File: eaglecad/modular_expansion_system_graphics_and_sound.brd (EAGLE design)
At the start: 81.4 x 100.5 mm, 63 parts, among them IC1_JOY2_BUF 74LS244N, IC2_GLU ATF22V10, IC3 74LS74N, IC8_JOY1_BUF 74LS244N, IC9-74HCU04 74LS04N, J1-INTERRUPTS INTERRUPTS, J1_ADDRESS_CON j1, J2-WAITS WAITS, J2_DATA_AND_POWER_CON j2, J3-VIDEO-OUT RCA, J4-AUDIO-LEFT RCA, J5-AUDIO-RIGHT RCA, Q2 2N2222, U11_SND1 SN76489, U1_TMS_RAM TMS4416, U2_VDP TMS9118, U3_TMS_RAM TMS4416, U4_SND2 SN76489, U5_SND3 SN76489, U6_SND4 SN76489, Y1 OSC1-CPP-4

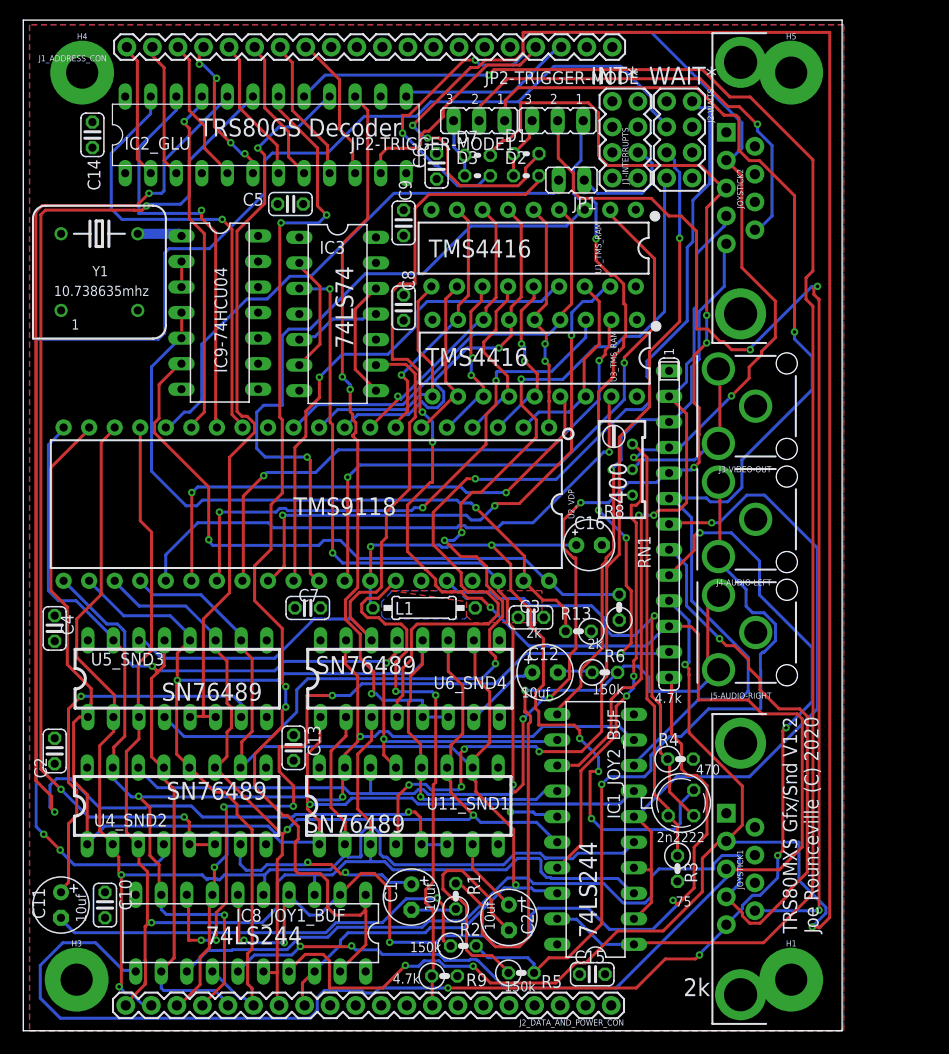
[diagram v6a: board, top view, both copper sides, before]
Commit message: joystick pin fixes to match old alphastick
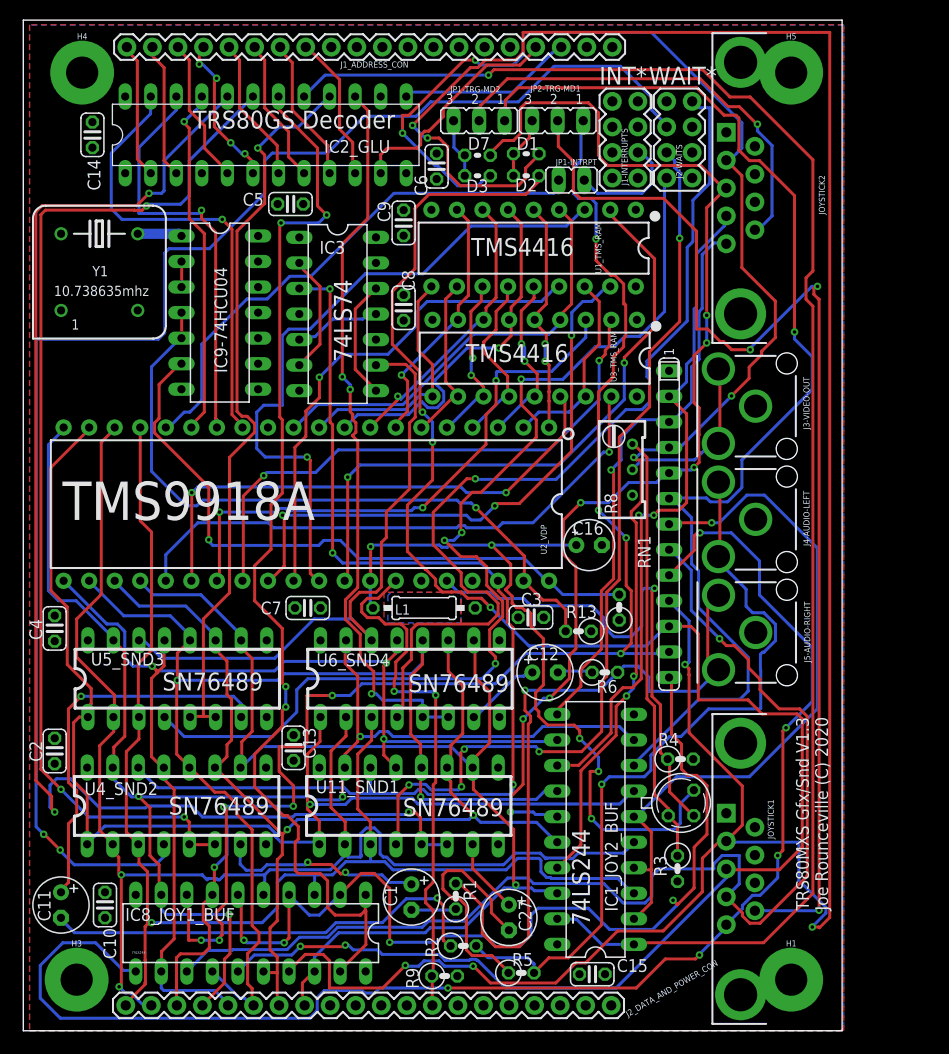
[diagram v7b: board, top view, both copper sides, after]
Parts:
- JP1-TRG-MD2: value (none) -> JP1
- JP2-TRG-MD1: value (none) -> JP2
- renumbered JP1 to JP1-INTRPT, JP2-TRIGGER-MODE to JP2-TRG-MD1, JP2-TRIGGER-MODE1 to JP1-TRG-MD2
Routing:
- net COMVID: track 46.1 -> 52.1 mm
- net DOWN: track 184.1 -> 182.3 mm
- net D2: track 138.4 -> 140.1 mm
- net RIGHT1: track 56.5 -> 57.3 mm
- net D3: track 138.3 -> 139.1 mm
- net 5_BIT_TRIGGER_LINE: track 139.8 -> 140.4 mm
- net D6: track 103.9 -> 104.5 mm
- net D7: track 111.1 -> 111.6 mm
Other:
- board text added: "TMS9918A"
- board text added: "TRS80MXS Gfx/Snd V1.3 Joe Rounceville (C) 2020"
- board text removed: "10uf"
- board text removed: "150k"
- board text removed: "2k"
- board text removed: "2n2222"
- board text removed: "4.7k"
- board text removed: "400"
- board text removed: "470"
- board text removed: "75"
- board text removed: "TMS9118"
- board text removed: "TRS80MXS Gfx/Snd V1.2 Joe Rounceville (C) 2020"

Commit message: updated graphics board to make joysticks compatible with old games
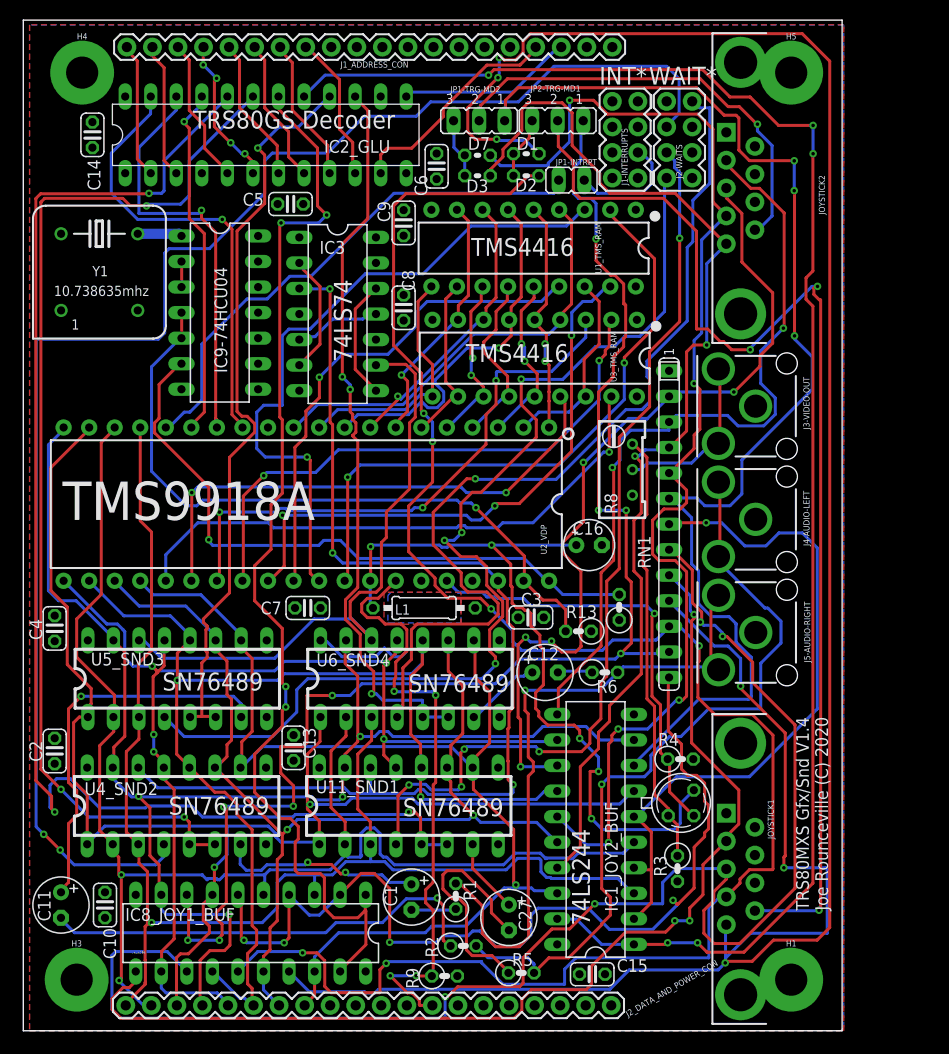
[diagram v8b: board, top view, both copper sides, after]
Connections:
- net JOY1_IN_ENABLE_N1 renamed JOY2_IN_ENABLE_N
- net N$11 renamed TIED-HIGH-1
- net N$20 renamed TIED-HIGH-2
- net DOWN: now also JOYSTICK1.4; no longer JOYSTICK1.3
- net DOWN1: now also JOYSTICK2.4; no longer JOYSTICK2.3
- net LEFT: now also JOYSTICK1.3; no longer JOYSTICK1.4
- net LEFT1: now also JOYSTICK2.3; no longer JOYSTICK2.4
- net RIGHT: now also JOYSTICK1.2; no longer JOYSTICK1.5
- net RIGHT1: now also JOYSTICK2.2; no longer JOYSTICK2.5
- net UP: now also JOYSTICK1.5; no longer JOYSTICK1.2
- net UP1: now also JOYSTICK2.5; no longer JOYSTICK2.2
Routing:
- net RIGHT: track 144.0 -> 108.2 mm, vias 5 -> 3
- net UP1: track 144.8 -> 109.4 mm, vias 6 -> 2
- net LEFT: track 119.0 -> 144.5 mm, vias 1 -> 4
- net RIGHT1: track 57.3 -> 77.5 mm, vias 1 -> 2
- net LEFT1: track 67.6 -> 85.4 mm, vias 2 -> 5
- net VCC: track 0.00 -> 10.2 mm
- net COMVID: track 52.1 -> 44.1 mm
- net SYSRES*: track 53.0 -> 59.9 mm, vias 2 -> 4
- net DOWN1: track 115.5 -> 120.4 mm, vias 7 -> 5
- net 5_BIT_TRIGGER_LINE_2: track 115.2 -> 119.7 mm, vias 1 -> 3
- net UP: track 257.7 -> 254.0 mm
- net SND2_READY: track 148.2 -> 151.8 mm
- net DOWN: track 182.3 -> 185.8 mm, vias 5 -> 6
- net N$24: track 68.0 -> 65.3 mm
- net JOY2_IN_ENABLE_N: track 157.5 -> 159.7 mm, vias 1 -> 5
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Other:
- board text added: "TRS80MXS Gfx/Snd V1.4 Joe Rounceville (C) 2020"
- board text removed: "TRS80MXS Gfx/Snd V1.3 Joe Rounceville (C) 2020"
